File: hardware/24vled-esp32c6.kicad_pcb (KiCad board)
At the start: 2 copper layers, 27.2 x 96.1 mm, 25 parts, among them J1 2601-1106, J2 Conn_01x02_Pin, Q1 AO3400A, Q2 AO3400A, Q3 AO3400A, Q4 AO3400A, Q5 AO3400A, U1 R-78E5.0-1.0

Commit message: change to 3.5mm file
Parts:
- C3: footprint Capacitor_THT:CP_Radial_D8.0mm_P5.00mm -> Capacitor_THT:CP_Radial_D8.0mm_P3.50mm

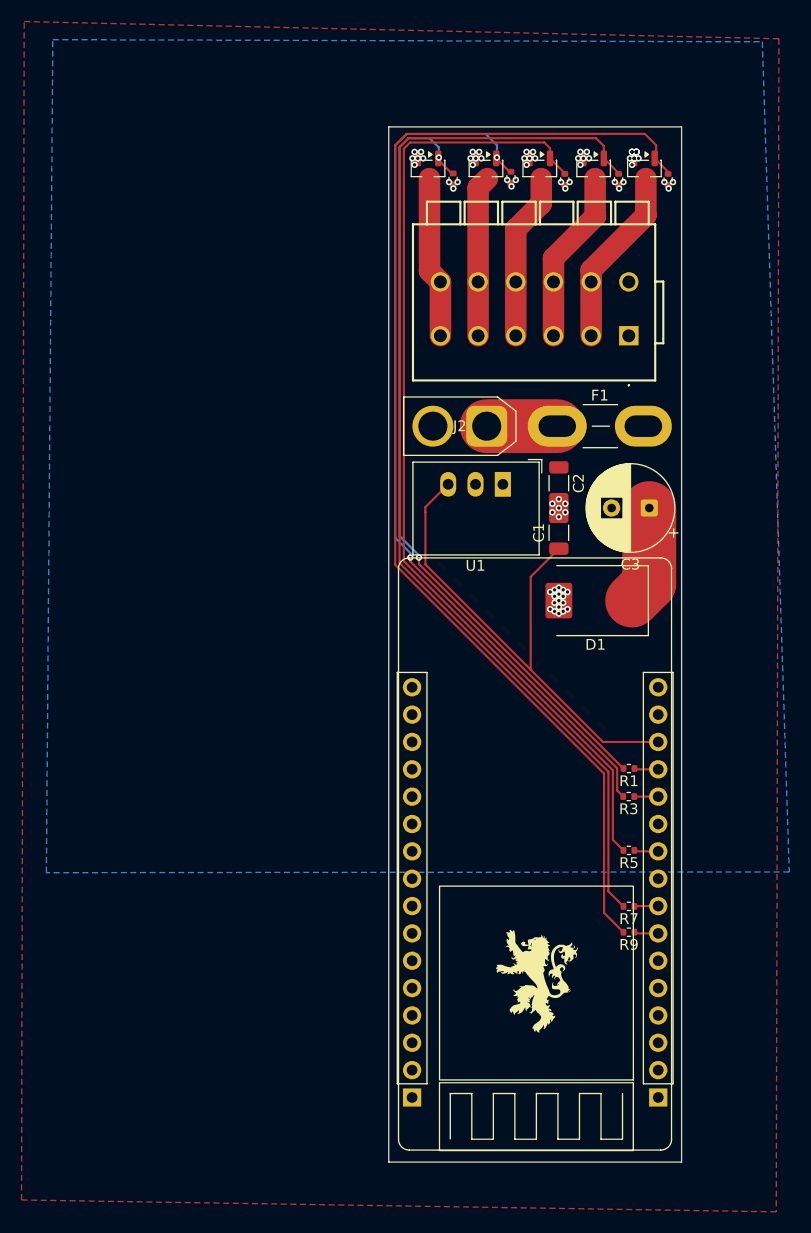
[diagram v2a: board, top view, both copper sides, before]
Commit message: add m.2 style cutout
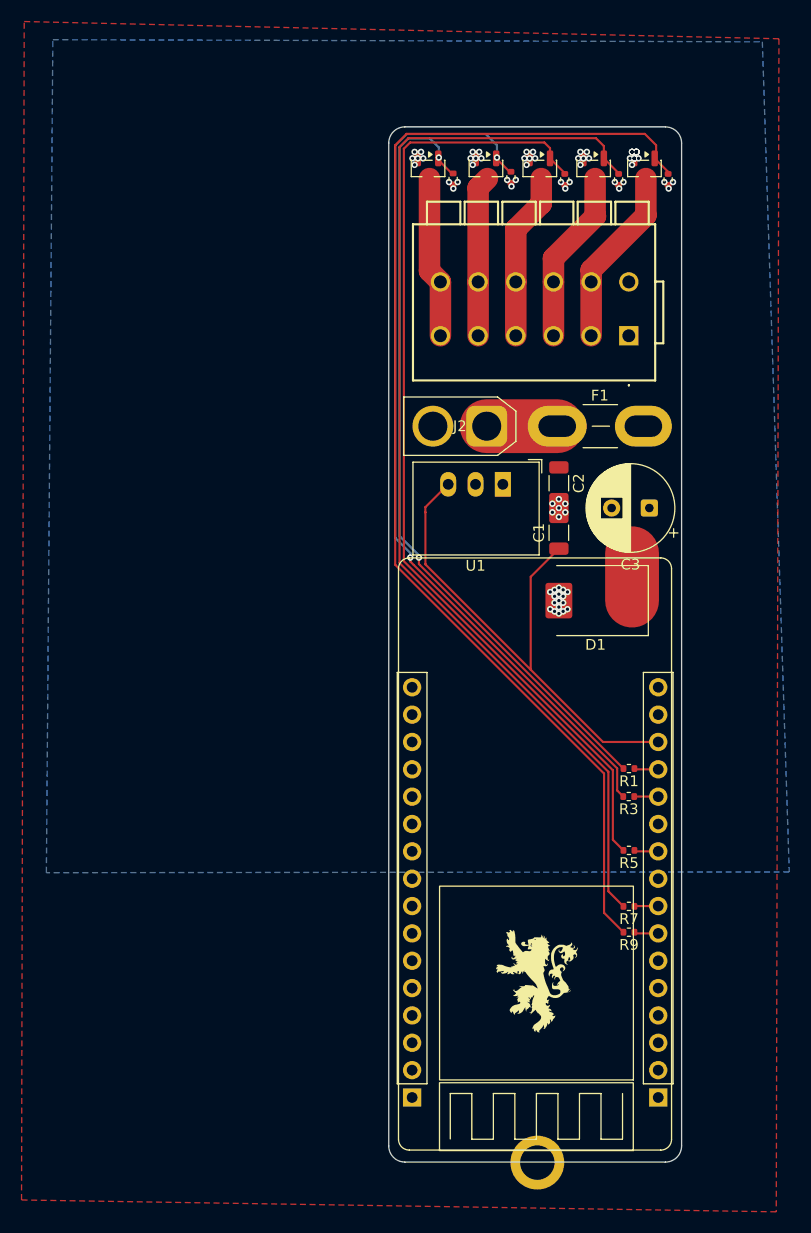
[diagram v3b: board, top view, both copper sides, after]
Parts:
- added REF**: MountingHole_3.2mm_M3, MountingHole:MountingHole_3.2mm_M3, F.Cu at (150.8, 131.0)
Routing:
- net +24V: track 9.26 -> 4.40 mm
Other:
- outline, holes or cut-outs redrawn
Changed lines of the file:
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@@
 		)
 	)
+	(footprint "MountingHole:MountingHole_3.2mm_M3"
+		(layer "F.Cu")
+		(at 150.8 131)
+		(descr "Mounting Hole 3.2mm, M3, no annular, generated by kicad-footprint-generator mountinghole.py")
+		(tags "mountinghole M3")
+		(property "Reference" "REF**"
+			(at 0 -4.15 0)
+			(layer "F.SilkS")
+			(hide yes)
+			(effects
+				(font
+					(size 1 1)
+					(thickness 0.15)
+				)
+			)
+		)
+		(property "Value" "MountingHole_3.2mm_M3"
+			(at 0 4.15 0)
+			(layer "F.Fab")
+			(effects
+				(font
+					(size 1 1)
+					(thickness 0.15)
+				)
+			)
+		)
+		(property "Datasheet" ""
+			(at 0 0 0)
+			(layer "F.Fab")
+			(hide yes)
+			(effects
+				(font
+					(size 1.27 1.27)
+					(thickness 0.15)
+				)
+			)
+		)
+		(property "Description" ""
+			(at 0 0 0)
+			(layer "F.Fab")
+			(hide yes)
+			(effects
+				(font
+					(size 1.27 1.27)
+					(thickness 0.15)
+				)
+			)
+		)
+		(attr exclude_from_pos_files exclude_from_bom)
+		(fp_circle
+			(center 0 0)
+			(end 3.2 0)
+			(stroke
+				(width 0.15)
+				(type solid)
+			)
+			(fill no)
+			(layer "Cmts.User")
+		)
+		(fp_circle
+			(center 0 0)
+			(end 3.45 0)
+			(stroke
+				(width 0.05)
+				(type solid)
+			)
+			(fill no)
+			(layer "F.CrtYd")
+		)
+		(fp_text user "${REFERENCE}"
+			(at 0 0 0)
+			(layer "F.Fab")
+			(effects
+				(font
+					(size 1 1)
+					(thickness 0.15)
+				)
+			)
+		)
+		(pad "" thru_hole circle
+			(at 0 0)
+			(size 5 5)
+			(drill 3.2)
+			(layers "*.Cu" "*.Mask")
+			(remove_unused_layers no)
+			(clearance 0)
+		)
+		(embedded_fonts no)
+	)
 	(footprint "Resistor_SMD:R_0402_1005Metric"
 		(layer "F.Cu")
@@
 		(net 1)
 	)
-	(gr_rect
-		(start 137 34.8)
-		(end 164.2 130.95)
+	(gr_arc
+		(start 162.7 34.8)
+		(mid 163.76066 35.23934)
+		(end 164.2 36.3)
+		(stroke
+			(width 0.05)
+			(type default)
+		)
+		(layer "Edge.Cuts")
+	)
+	(gr_line
+		(start 137 129.45)
+		(end 137 36.3)
+		(stroke
+			(width 0.05)
+			(type default)
+		)
+		(layer "Edge.Cuts")
+	)
+	(gr_line
+		(start 164.2 36.3)
+		(end 164.2 129.45)
+		(stroke
+			(width 0.05)
+			(type default)
+		)
+		(layer "Edge.Cuts")
+	)
+	(gr_arc
+		(start 137 36.3)
+		(mid 137.43934 35.23934)
+		(end 138.5 34.8)
+		(stroke
+			(width 0.05)
+			(type default)
+		)
+		(layer "Edge.Cuts")
+	)
+	(gr_line
+		(start 162.7 130.95)
+		(end 138.5 130.95)
+		(stroke
+			(width 0.05)
+			(type default)
+		)
+		(layer "Edge.Cuts")
+	)
+	(gr_arc
+		(start 164.2 129.45)
+		(mid 163.76066 130.51066)
+		(end 162.7 130.95)
+		(stroke
+			(width 0.05)
+			(type default)
+		)
+		(layer "Edge.Cuts")
+	)
+	(gr_arc
+		(start 138.5 130.95)
+		(mid 137.43934 130.51066)
+		(end 137 129.45)
+		(stroke
+			(width 0.05)
+			(type default)
+		)
+		(layer "Edge.Cuts")
+	)
+	(gr_line
+		(start 138.5 34.8)
+		(end 162.7 34.8)
 		(stroke
 			(width 0.05)
 			(type default)
 		)
-		(fill no)
 		(layer "Edge.Cuts")
 	)
@@
 	)
 	(segment
-		(start 161.199 77.201)
-		(end 161.199 70.2)
-		(width 5)
-		(layer "F.Cu")
-		(net 2)
-	)
-	(segment
 		(start 159.6 78.8)
-		(end 161.199 77.201)
+		(end 159.6 74.4)
 		(width 5)
 		(layer "F.Cu")
